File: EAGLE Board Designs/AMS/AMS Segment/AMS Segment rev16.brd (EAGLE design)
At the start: 275.2 x 86 mm, 310 parts, among them J0 CONNECTOR-1_5222_, J1 CONNECTOR-1_5222_, J10 CONNECTOR-1_5222_, J11 CONNECTOR-1_5222_, J12 CONNECTOR-1_5222_, J13 CONNECTOR-1_5222_, J14 CONNECTOR-1_5222_, J15 CONNECTOR-1_5222_, J16 CONNECTOR-1_5222_, J17 CONNECTOR-1_5222_, J18 CONNECTOR-1_5222_, J2 CONNECTOR-1_5222_, J27 CONNECTOR-2_MICROFIT_SMD_RIGH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, J28 CONNECTOR-2_MICROFIT_SMD_RIGH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, J29 CONNECTOR-1_5222_, J3 CONNECTOR-1_5222_, J30 CONNECTOR-1_5222_, J31 CONNECTOR-1_5222_, J32 CONNECTOR-2_MICROFIT_SMD_RIGH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, J33 CONNECTOR-2_MICROFIT_SMD_RIGH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, J34 CONNECTOR-2_MICROFIT_SMD_RIGH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, J35 CONNECTOR-2_MICROFIT_SMD_RIGH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, J37 CONNECTOR-2_MICROFIT_SMD_RIGH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, J38 CONNECTOR-2_MICROFIT_SMD_RIGH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, J39 CONNECTOR-2_MICROFIT_SMD_RIGH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, J4 CONNECTOR-1_5222_, J40 CONNECTOR-2_MICROFIT_SMD_RIGH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, J5 CONNECTOR-1_5222_, J6 CONNECTOR-1_5222_, J7 CONNECTOR-1_5222_, J8 CONNECTOR-1_5222_, J9 CONNECTOR-1_5222_, T1 TRANSFORMER_HM2112ZNLT, U1 LTC6811-2, U2 LTC6811-2, U3 SHT31-ARP-B, U4 SHT31-ARP-B, U5 LT3990-5, U6 LT3990-5

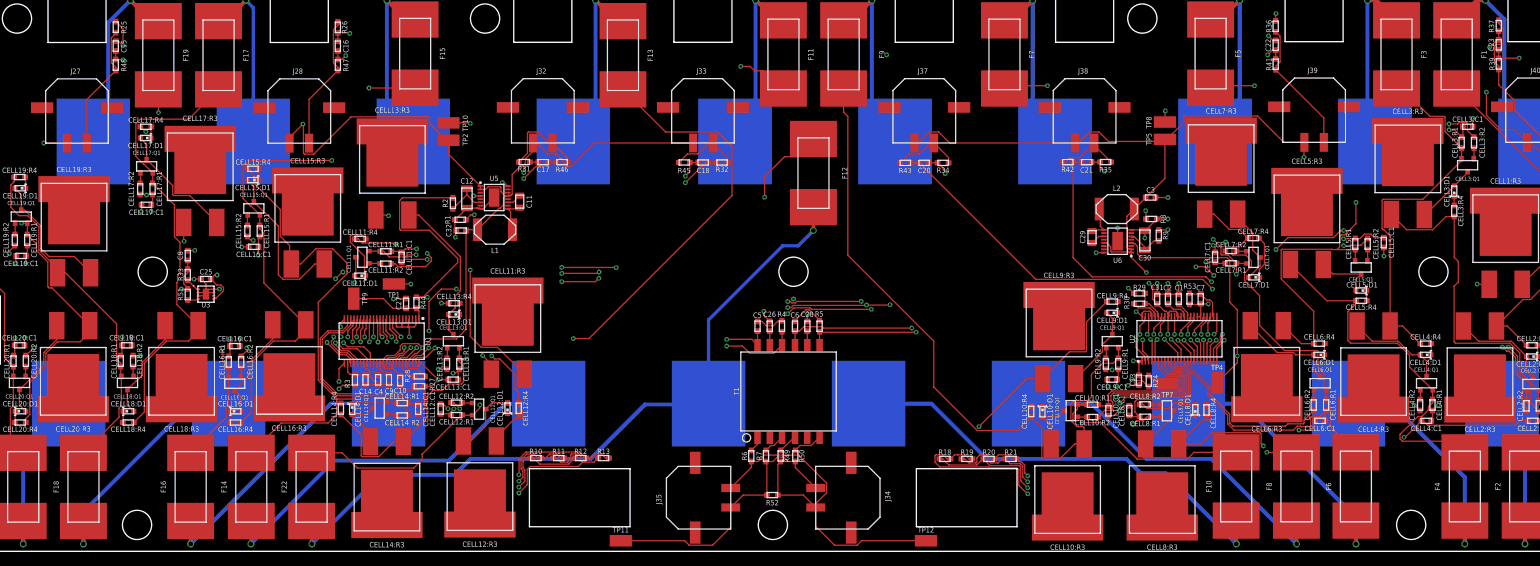
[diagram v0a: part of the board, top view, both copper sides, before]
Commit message: fixed some routing issues.
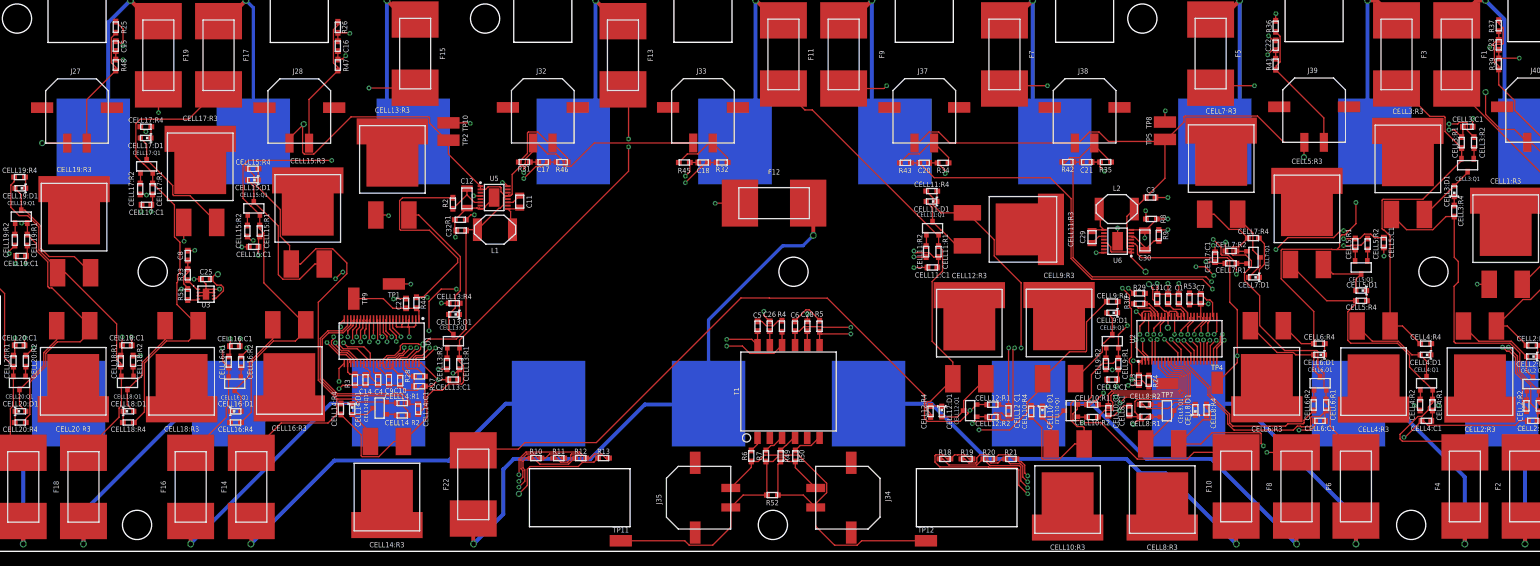
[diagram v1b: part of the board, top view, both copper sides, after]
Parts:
- moved CELL11:D1 88.8 mm to (161.3, -32.1)
- moved CELL11:R4 88.3 mm to (161.4, -30.5)
- moved CELL11:Q1 87.9 mm to (161.5, -36.2), turned to 0 degrees
- moved CELL12:C1 87.5 mm to (173.2, -64.3), turned to 270 degrees
- moved CELL11:R1 85.1 mm to (162.4, -39.8), turned to 270 degrees
- moved CELL11:R2 83.2 mm to (160.5, -39.8), turned to 270 degrees
- moved CELL12:R2 82.6 mm to (170.8, -65.3), turned to 0 degrees
- moved CELL12:R1 82.6 mm to (170.8, -63.4), turned to 0 degrees
- moved CELL11:C1 81.8 mm to (161.5, -42.3), turned to 180 degrees
- moved CELL12:R3 76.0 mm to (167.2, -59.4), turned to 0 degrees
- moved CELL12:Q1 75.6 mm to (167.3, -64.3), turned to 90 degrees
- moved CELL11:R3 74.2 mm to (166.9, -36.4), turned to 270 degrees
- moved CELL12:D1 66.9 mm to (162.9, -64.5), turned to 270 degrees
- moved CELL12:R4 63.4 mm to (161.2, -64.4), turned to 90 degrees
- moved F22 24.9 mm to (90.8, -75.7)
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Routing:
- net V-L: track 277.7 -> 129.3 mm, vias 37 -> 35
- net SENSE10: track 185.9 -> 83.7 mm, vias 5 -> 3
- net C12L: track 122.0 -> 34.5 mm, vias 4 -> 2
- net S11L: track 136.7 -> 50.8 mm, vias 4 -> 2
- net S12L: track 121.1 -> 37.4 mm, vias 4 -> 2
- net C11L: track 132.9 -> 74.5 mm, vias 4 -> 2
- net SENSE11: track 123.6 -> 65.9 mm, vias 3 -> 0
- net CELL11:N$6: track 63.6 -> 10.4 mm, vias 2 -> 0
- net SENSE12: track 209.3 -> 158.9 mm, vias 6 -> 4
- net SENSE13: track 121.2 -> 86.6 mm
- net CC12: track 111.9 -> 92.9 mm
- net V-U: track 117.3 -> 108.1 mm
- net CELL11:N$7: track 9.82 -> 1.62 mm
- net SENSE9: track 106.4 -> 99.2 mm, vias 0 -> 2
- net GPIO1L: track 64.9 -> 70.3 mm
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
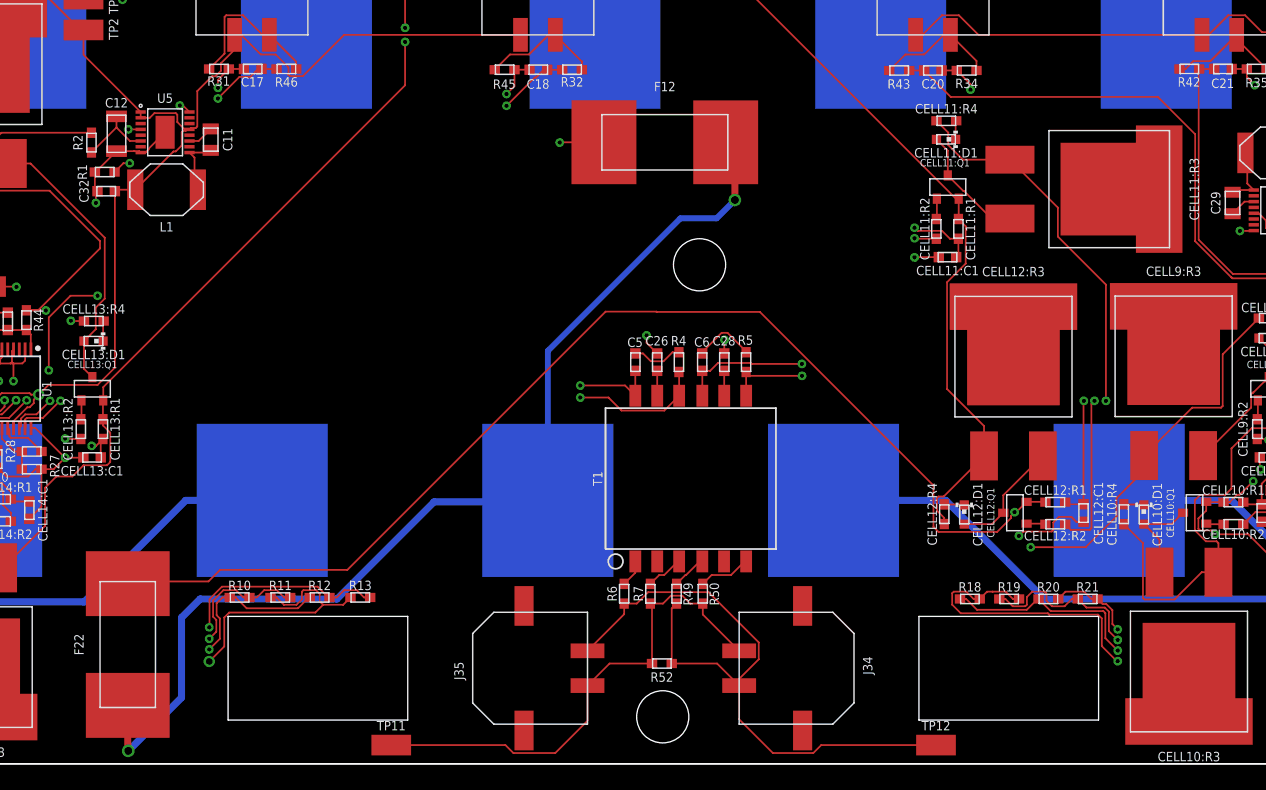
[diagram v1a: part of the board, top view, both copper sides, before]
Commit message: Updated plane divisions
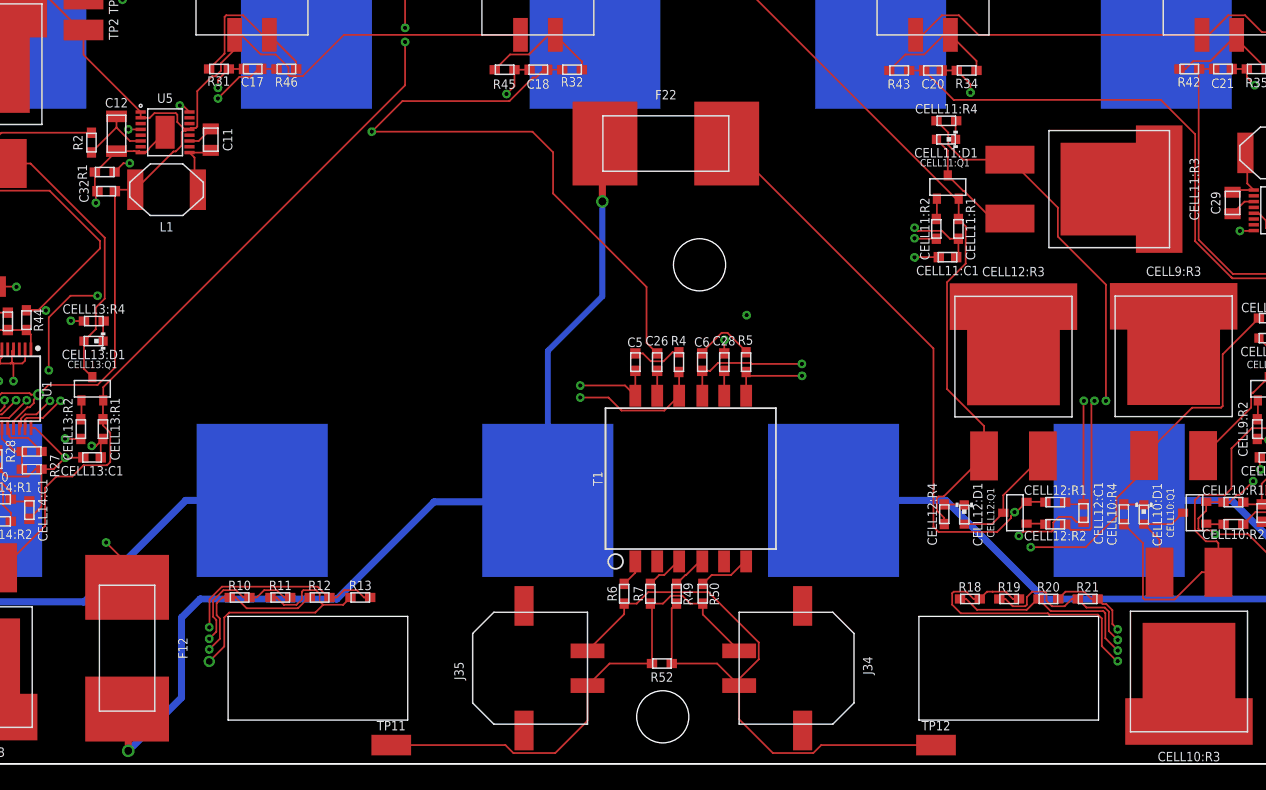
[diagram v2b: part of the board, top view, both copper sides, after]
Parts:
- moved F12 63.7 mm to (90.7, -76.0), turned to 90 degrees
- moved F22 63.4 mm to (137.2, -32.5), turned to 0 degrees
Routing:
- net V-U: track 108.1 -> 156.9 mm, vias 24 -> 23
- net SENSE12: track 158.9 -> 110.4 mm
- net CC12: track 92.9 -> 85.6 mm
- net V-L: track 129.3 -> 132.4 mm, vias 35 -> 36

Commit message: actually ran the correct DRC and fixed 177 errors
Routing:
- net VREGL: track 259.4 -> 261.2 mm
- net SENSE5: track 87.7 -> 89.2 mm
- net SENSE9: track 99.2 -> 98.0 mm
- net GPIO1L: track 70.3 -> 69.2 mm
- net DRVL: track 53.1 -> 52.0 mm
- net C11L: track 74.5 -> 75.4 mm
- net C2L: track 77.4 -> 78.3 mm
- net IPL: track 57.7 -> 58.6 mm
- net V-L: track 132.4 -> 133.3 mm
- net IML: track 62.9 -> 63.6 mm
- net S11L: track 50.8 -> 51.5 mm
- net SENSE7: track 152.3 -> 152.9 mm
- net SENSE8: track 100.2 -> 100.8 mm
- net S1U: track 69.7 -> 70.3 mm

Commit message: fixed small things
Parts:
- moved F22 4.62 mm to (141.7, -31.8)
- moved C31 0.10 mm to (196.2, -47.1)
- moved TP7 0.08 mm to (197.6, -60.2)
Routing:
- net CC12: track 85.6 -> 88.2 mm
- net VREGL: track 261.2 -> 262.5 mm
- net SENSE12: track 110.2 -> 109.0 mm
- net SENSE13: track 86.6 -> 87.5 mm
- net SENSE3: track 57.5 -> 58.3 mm
- net SENSE4: track 57.1 -> 57.8 mm
- net VREGU: track 271.9 -> 272.6 mm
- net V-U: track 156.9 -> 157.5 mm
- net S10L: track 23.2 -> 23.7 mm
- net V-L: track 133.3 -> 133.8 mm
- net SENSE2: track 60.1 -> 60.7 mm

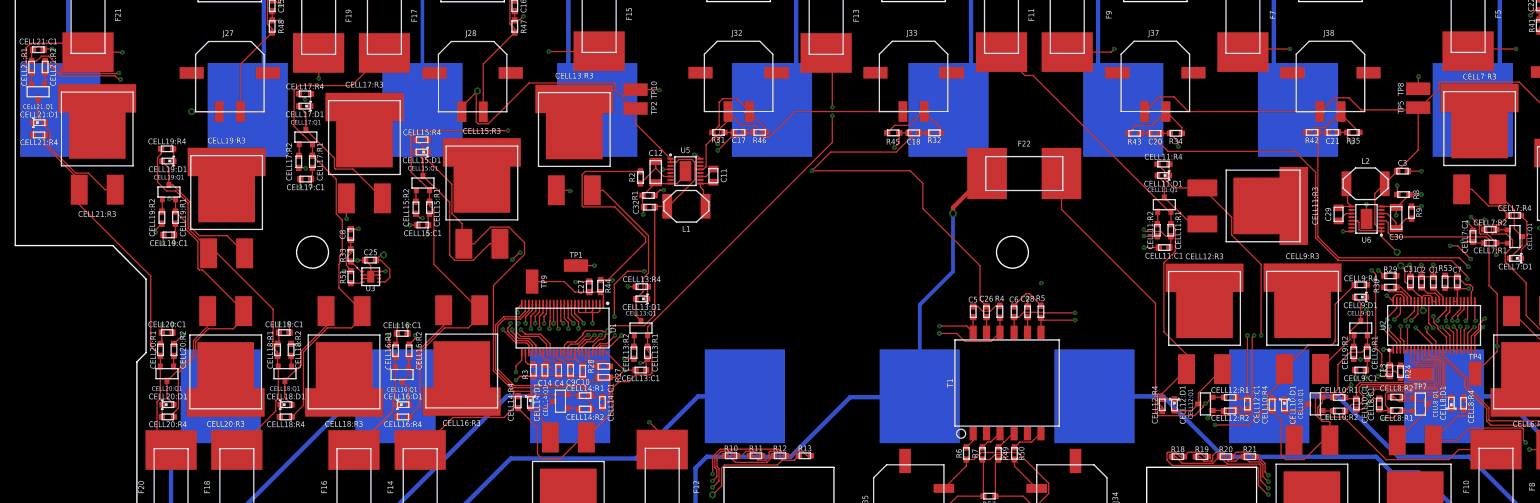
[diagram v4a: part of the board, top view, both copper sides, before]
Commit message: began updating discharge trace sizes
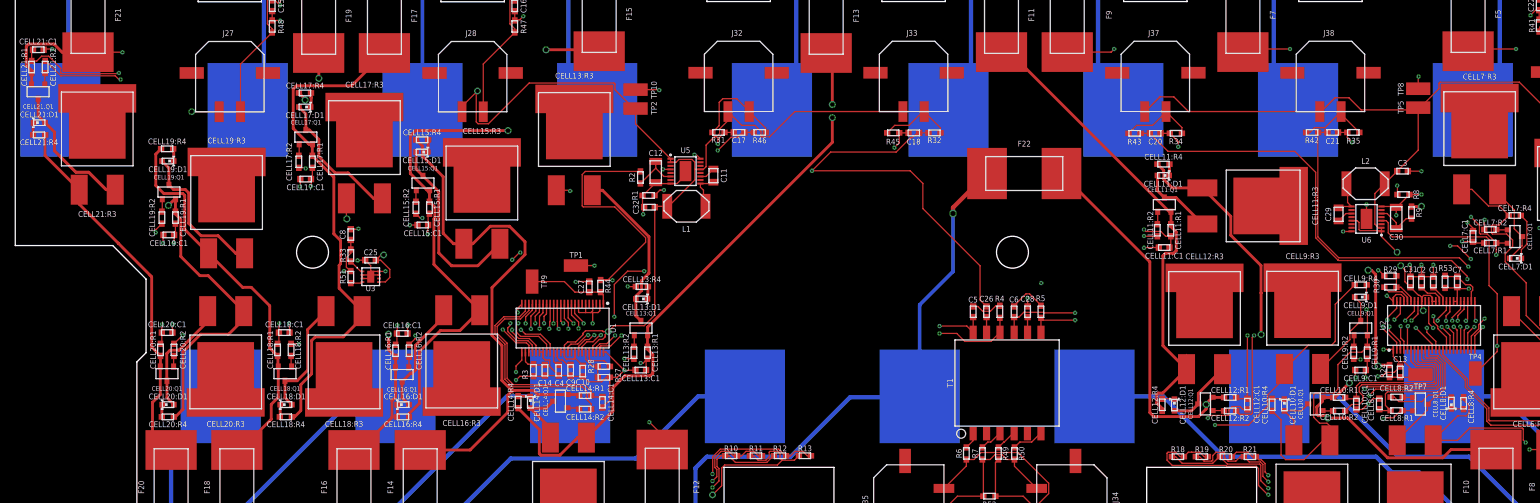
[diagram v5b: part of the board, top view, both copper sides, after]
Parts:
- moved R24 1.55 mm to (193.2, -59.7), turned to 90 degrees
- moved C13 1.48 mm to (194.7, -59.8), turned to 90 degrees
- moved CELL17:D1 0.13 mm to (40.3, -22.5)
- moved CELL17:R4 0.13 mm to (40.3, -20.5)
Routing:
- net CELL21:N$6: track 19.2 -> 29.9 mm
- net CELL14:N$6: track 8.95 -> 16.5 mm
- net V+L: track 8.70 -> 13.3 mm
- net SENSE19: track 80.7 -> 84.8 mm
- net SENSE11: track 65.9 -> 69.3 mm
- net V-L: track 133.8 -> 135.8 mm
- net SENSE18: track 53.6 -> 55.6 mm
- net SENSE21: track 153.4 -> 155.2 mm
- net SENSE14: track 79.3 -> 80.8 mm
- net SENSE15: track 84.4 -> 85.8 mm
- net CELL15:N$6: track 24.9 -> 26.2 mm
- net SENSE12: track 109.0 -> 107.8 mm
- net SENSE16: track 63.0 -> 64.2 mm
- net CELL18:N$6: track 16.1 -> 17.0 mm
- net SENSE17: track 71.6 -> 72.5 mm
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
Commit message: discharge branch size updates complete
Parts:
- moved CELL4:C1 0.25 mm to (237.5, -66.1)
- moved R24 0.13 mm to (193.1, -59.7)
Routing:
- net CELL21:N$6: track 29.9 -> 19.1 mm
- net SENSE8: track 101.2 -> 110.2 mm
- net SENSE21: track 155.2 -> 146.7 mm
- net SENSE7: track 153.1 -> 159.5 mm
- net SENSE1: track 58.0 -> 62.7 mm
- net SENSE10: track 83.5 -> 81.2 mm
- net SENSE5: track 89.2 -> 87.1 mm
- net SENSE11: track 69.3 -> 67.2 mm
- net SENSE2: track 60.7 -> 58.6 mm
- net SENSE4: track 57.8 -> 59.8 mm
- net DRVL: track 52.2 -> 50.2 mm
- net SENSE3: track 58.3 -> 60.2 mm
- net V+L: track 13.3 -> 11.9 mm
- net SENSE6: track 55.6 -> 57.0 mm
- net GPIO3L: track 56.9 -> 57.7 mm
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
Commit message: Made board compliant with all 4 main DRCs as well as default DRC
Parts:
- moved CELL17:D1 0.36 mm to (40.3, -22.8)
- moved CELL7:D1 0.30 mm to (211.3, -43.8)
- moved CELL13:C1 0.20 mm to (87.7, -59.7)
- moved CELL19:R1 0.20 mm to (22.1, -38.3)
- moved CELL19:R2 0.20 mm to (20.2, -38.3)
- moved CELL17:R2 0.15 mm to (39.3, -30.2)
- moved CELL9:R1 0.13 mm to (190.2, -57.1)
- moved CELL4:C1 0.10 mm to (237.6, -66.1)
- moved CELL19:Q1 0.08 mm to (21.2, -34.4)
- moved F14 0.08 mm to (56.6, -76.0)
- moved F16 0.08 mm to (47.2, -76.0)
- moved F18 0.08 mm to (30.7, -76.0)
- moved F20 0.08 mm to (21.5, -76.0)
- moved C25 0.05 mm to (49.6, -44.0)
- moved CELL15:C1 0.05 mm to (56.9, -39.1)
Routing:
- net VREGU: track 273.1 -> 277.9 mm
- net SENSE8: track 110.2 -> 113.9 mm
- net N$67: track 62.6 -> 65.6 mm
- net V-L: track 136.0 -> 138.2 mm
- net GPIO3L: track 57.7 -> 55.6 mm
- net S1U: track 70.3 -> 72.0 mm
- net VREGL: track 262.5 -> 264.3 mm
- net SENSE12: track 107.6 -> 109.4 mm
- net V-U: track 157.5 -> 159.1 mm
- net C1L: track 91.9 -> 93.4 mm
- net DRVU: track 69.7 -> 71.2 mm
- net GPIO5L: track 85.1 -> 83.8 mm
- net IPL: track 58.6 -> 59.9 mm
- net IPU: track 82.3 -> 83.6 mm
- net SENSE6: track 57.0 -> 58.2 mm
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
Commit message: add silkscreen
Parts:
- added U$10, U$17, U$18, U$19, U$20, U$21, U$22, U$26, U$8, U$9: (no value), HyTechAesthetics:HV_0.50"
- added U$2: (no value), HyTechAesthetics:LOGO_HYTECH_1.0"
- added U$23, U$24: (no value), HyTechAesthetics:HV_1.00"
- added U$25, U$27: (no value), HyTechAesthetics:DANGER_HIGH_VOLTAGE
- added U$3: (no value), HyTechAesthetics:LOGO_GT_0.50"
- added U$7: (no value), HyTechAesthetics:NUMBER
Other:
- board text added: "HyTech Racing 2021 AMS Segment rev16 Designed by Noah Bruckner"
